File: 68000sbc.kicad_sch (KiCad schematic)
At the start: 45 parts, among them J1 USB_B, J2 5V FTDI SERIAL, J3 RTC (SparkFun BOB-10160), J4 CFCARD/IDE, J5 EXPANSION (F.Cu), J6 EXPANSION (B.Cu), SW1 RESET, SW2 BTN1, U1 74HC139, U2 74HC14, U3 TMP68HC000P-12, U4 AS6C4008-55PCN, U5 28C256, U6 AS6C4008-55PCN, U7 28C256, U8 TL16C550, X1 12MHz, X2 12MHz

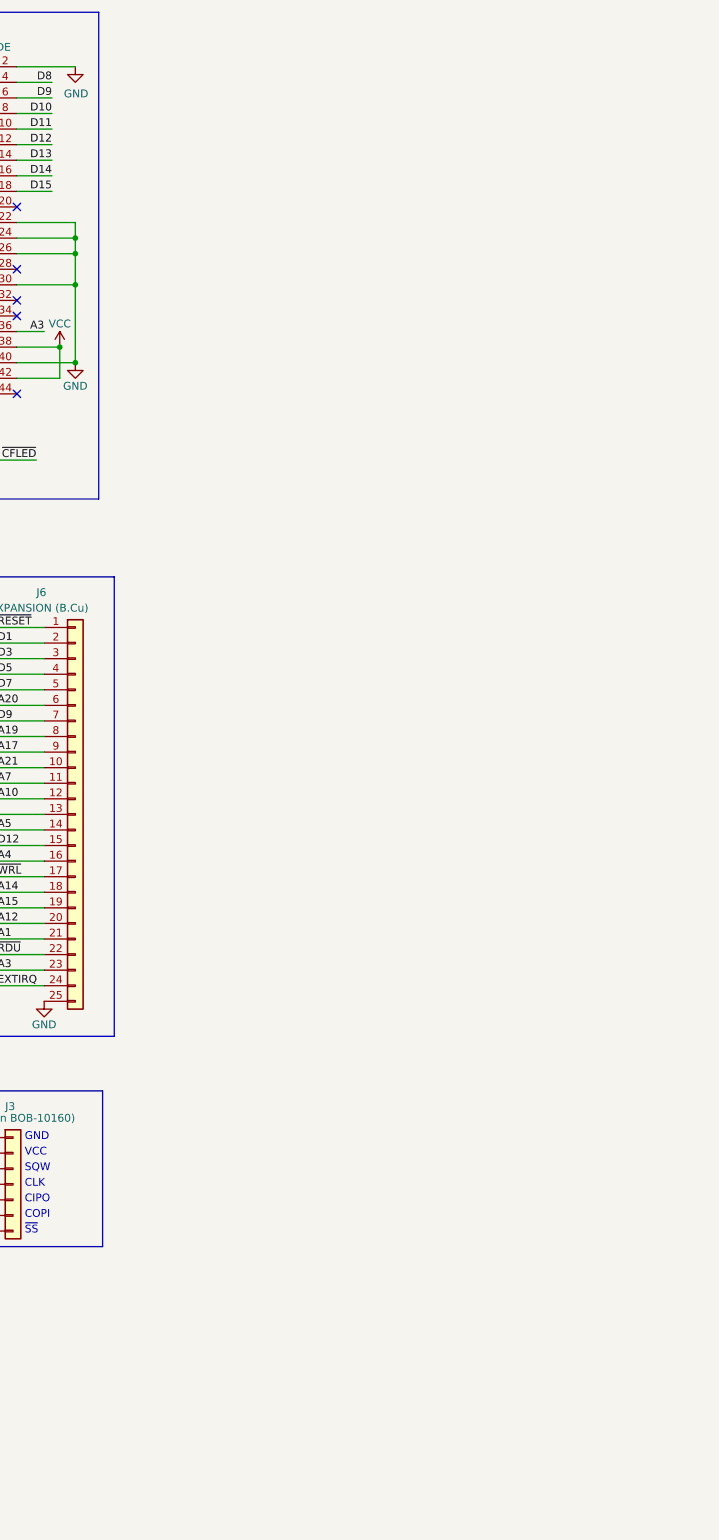
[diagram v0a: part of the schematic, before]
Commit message: start drawing expansion slot schematic
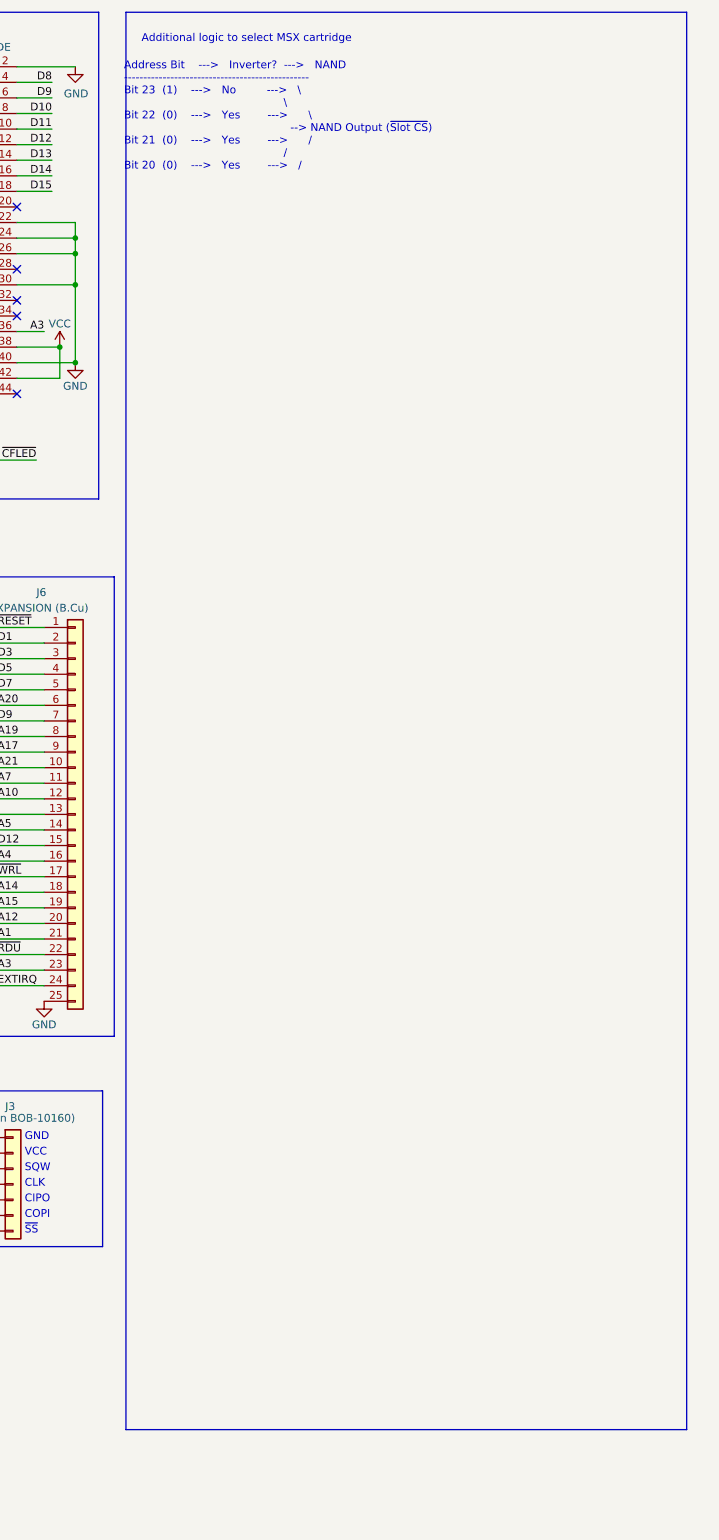
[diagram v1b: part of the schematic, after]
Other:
- note added: "Additional logic to select MSX cartridge"
- note added: "Address Bit ---> Inverter? ---> NAND ------------------------------------------------ Bit 23 (1) ---> No ---> \ \ Bit 22 (0) ---> Yes ---> \ --> NAND Output (~{Slot CS}) Bit 21 (0) ---> Yes ---> / / Bit 20 (0) ---> Yes ---> /"
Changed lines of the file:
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@@
     (stroke (width 0) (type default))
+  )
+  (rectangle (start 312.42 17.78) (end 403.86 248.92)
+    (stroke (width 0) (type default))
+    (fill (type none))
   )
   (text "MCR[1]" (at 187.325 186.055 0)
@@
     (effects (font (size 1.27 1.27)) (justify left bottom))
   )
+  (text "    Address Bit    --->   Inverter?  --->   NAND\n    ------------------------------------------------\n    Bit 23  (1)    --->   No         --->   \\\n                                                   \\\n    Bit 22  (0)    --->   Yes        --->      \\\n                                                     --> NAND Output (~{Slot CS})\n    Bit 21  (0)    --->   Yes        --->      /\n                                                   /\n    Bit 20  (0)    --->   Yes        --->   /\n\n"
+    (at 309.88 45.72 0)
+    (effects (font (size 1.27 1.27)) (justify left bottom))
+  )
   (text "GND" (at 295.91 201.93 0)
     (effects (font (size 1.27 1.27)) (justify left bottom))
@@
     (effects (font (size 1.27 1.27)) (justify left bottom))
   )
+  (text "Additional logic to select MSX cartridge" (at 314.96 22.86 0)
+    (effects (font (size 1.27 1.27)) (justify left bottom))
+  )

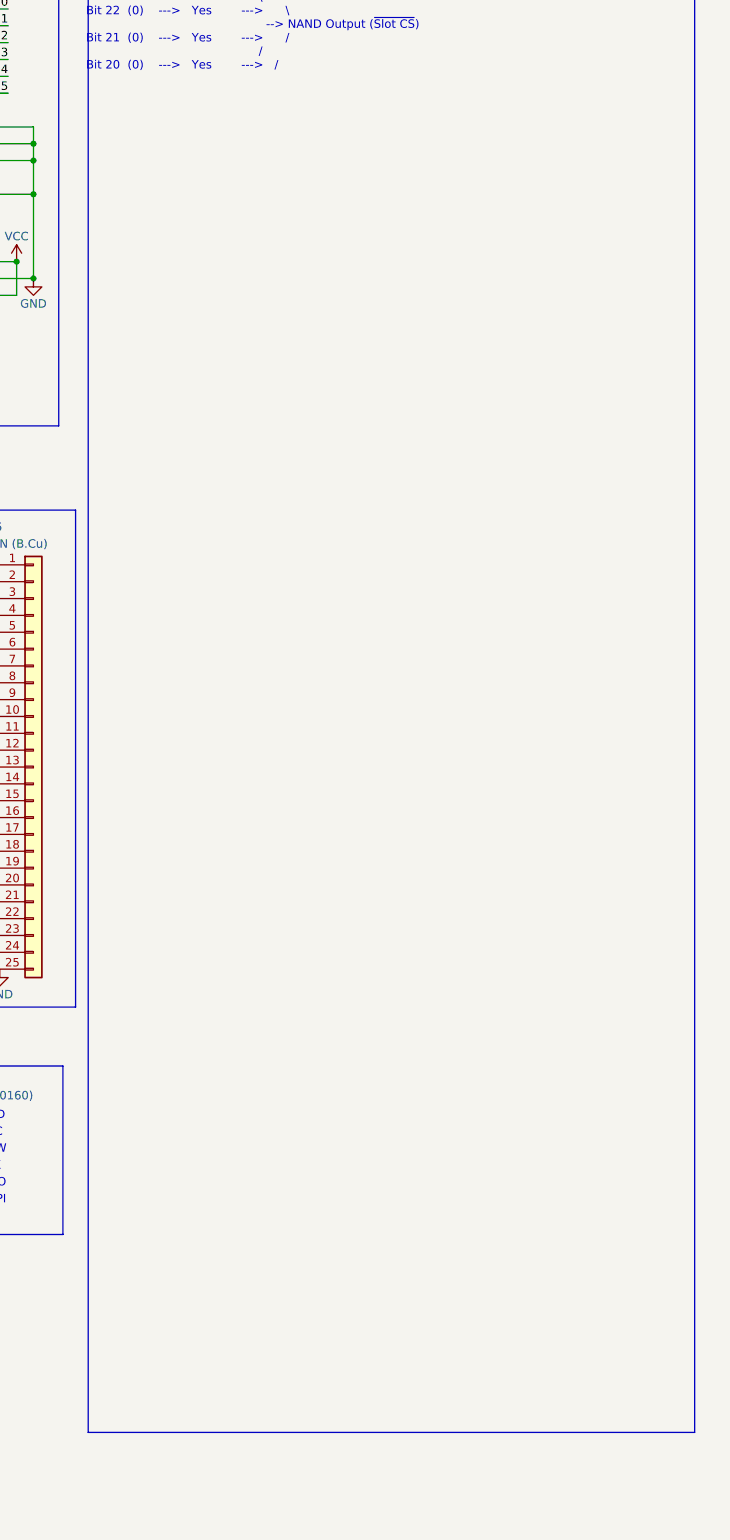
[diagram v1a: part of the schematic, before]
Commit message: hopefully working select circuit
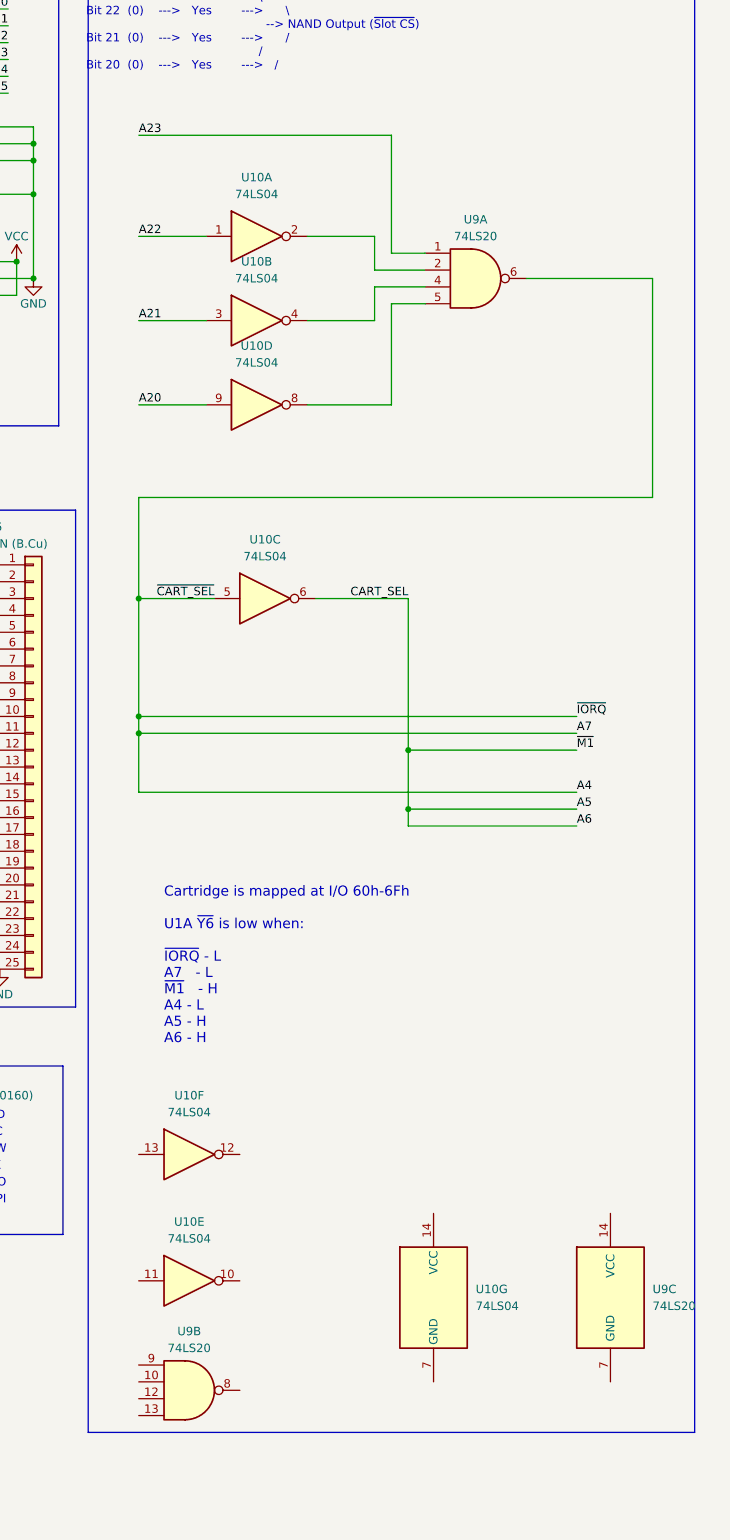
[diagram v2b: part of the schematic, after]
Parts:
- added U10: 74LS04, symbol 74xx:74LS04
- added U9: 74LS20, symbol 74xx:74LS20
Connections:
- net A6 is gone; now on net A5: J5.11 (Pin_11), U3.34 (A6), U4.7 (A5), U5.5 (A5), U6.7 (A5), U7.5 (A5)
- net A7 is gone; now on net A4: J6.11 (Pin_11), U3.35 (A7), U4.6 (A6), U5.4 (A6), U6.6 (A6), U7.4 (A6)
- net A20: now also U10.9
- net A21: now also U10.3
- net A22: now also U10.1
- net A23: now also U9.1
- net A4: now also U10.5, U9.6
- net A5: now also U10.6
- new net: U10.4, U9.4
- new net: U10.2, U9.2
- new net: U10.8, U9.5
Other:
- note added: "Cartridge is mapped at I/O 60h-6Fh U1A ~{Y6} is low when: ~{IORQ} - L A7 - L ~{M1} - H A4 - L A5 - H A6 - H"
